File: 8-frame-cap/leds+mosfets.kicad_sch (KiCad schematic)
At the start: 113 parts, among them T1 PHPT610035PKX, T2 PHPT610035PKX, T3 PHPT610035PKX, T4 PHPT610035PKX, T5 PHPT610035PKX, T6 PHPT610035PKX, T7 PHPT610035PKX, U4 SN74AHCT32DBR, U5 SN74AHCT32DBR

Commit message: routed traces, reorganized, renamed
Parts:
- removed D2: 4, LED_SMD:LED_0603_1608Metric, symbol Device:LED
- removed D3, D5, D6: 56, LED_SMD:LED_0603_1608Metric, symbol Device:LED
- removed D4: 5, LED_SMD:LED_0603_1608Metric, symbol Device:LED
- added D10, D28, D52, D58, D64: 23, LED_SMD:LED_0805_2012Metric_Pad1.15x1.40mm_HandSolder, symbol Device:LED
- added D18, D36, D53, D54, D59, D60, D65, D66: 3, LED_SMD:LED_0805_2012Metric_Pad1.15x1.40mm_HandSolder, symbol Device:LED
- added D20, D56, D62: 12, LED_SMD:LED_0805_2012Metric_Pad1.15x1.40mm_HandSolder, symbol Device:LED
- added D43, D55, D61, D67: 1, LED_SMD:LED_0805_2012Metric_Pad1.15x1.40mm_HandSolder, symbol Device:LED
- added D51, D57, D63: 2, LED_SMD:LED_0805_2012Metric_Pad1.15x1.40mm_HandSolder, symbol Device:LED
- added R10, R14, R23, R32, R40, R48, R55, R63, R64, R65, R66, R67, R7, R8, R9: R_Small_US, Resistor_SMD:R_0603_1608Metric_Pad0.98x0.95mm_HandSolder, symbol Device:R_Small_US
- added T8: PHPT610035PKX, GRAD-CAP:PHPT610035PKX_TRANS-2PNP-100V-3A, symbol PHPT610035PKX_TRANS-2PNP-100V-3A:PHPT610035PKX
- added TP1, TP10, TP11, TP12, TP13, TP14, TP15, TP16, TP2, TP3, TP4, TP5, TP6, TP7, TP8, TP9: TestPoint, TestPoint:TestPoint_Loop_D3.80mm_Drill2.5mm, symbol testpoint:TestPoint
- D1, D8: footprint LED_SMD:LED_0603_1608Metric -> LED_SMD:LED_0805_2012Metric_Pad1.15x1.40mm_HandSolder
- D11, D30: value 6 -> 3; footprint LED_SMD:LED_0603_1608Metric -> LED_SMD:LED_0805_2012Metric_Pad1.15x1.40mm_HandSolder
- D12, D23, D24: value 67 -> 3; footprint LED_SMD:LED_0603_1608Metric -> LED_SMD:LED_0805_2012Metric_Pad1.15x1.40mm_HandSolder
- D13: value 56 -> 1; footprint LED_SMD:LED_0603_1608Metric -> LED_SMD:LED_0805_2012Metric_Pad1.15x1.40mm_HandSolder
- D14: value 6 -> 12; footprint LED_SMD:LED_0603_1608Metric -> LED_SMD:LED_0805_2012Metric_Pad1.15x1.40mm_HandSolder
- D15: value 6 -> 2; footprint LED_SMD:LED_0603_1608Metric -> LED_SMD:LED_0805_2012Metric_Pad1.15x1.40mm_HandSolder
- D16: value 1 -> 23; footprint LED_SMD:LED_0603_1608Metric -> LED_SMD:LED_0805_2012Metric_Pad1.15x1.40mm_HandSolder
- D17, D42: value 23 -> 3; footprint LED_SMD:LED_0603_1608Metric -> LED_SMD:LED_0805_2012Metric_Pad1.15x1.40mm_HandSolder
- D19: value 23 -> 1; footprint LED_SMD:LED_0603_1608Metric -> LED_SMD:LED_0805_2012Metric_Pad1.15x1.40mm_HandSolder
- D2: renamed from D10; footprint LED_SMD:LED_0603_1608Metric -> LED_SMD:LED_0805_2012Metric_Pad1.15x1.40mm_HandSolder
- D21: value 67 -> 2; footprint LED_SMD:LED_0603_1608Metric -> LED_SMD:LED_0805_2012Metric_Pad1.15x1.40mm_HandSolder
- D22: value 7 -> 23; footprint LED_SMD:LED_0603_1608Metric -> LED_SMD:LED_0805_2012Metric_Pad1.15x1.40mm_HandSolder
- D25: value 6 -> 1; footprint LED_SMD:LED_0603_1608Metric -> LED_SMD:LED_0805_2012Metric_Pad1.15x1.40mm_HandSolder
- D26: value 32 -> 12; footprint LED_SMD:LED_0603_1608Metric -> LED_SMD:LED_0805_2012Metric_Pad1.15x1.40mm_HandSolder
- D27: value 1 -> 2; footprint LED_SMD:LED_0603_1608Metric -> LED_SMD:LED_0805_2012Metric_Pad1.15x1.40mm_HandSolder
- D29: value 7 -> 3; footprint LED_SMD:LED_0603_1608Metric -> LED_SMD:LED_0805_2012Metric_Pad1.15x1.40mm_HandSolder
- D3: renamed from D20; footprint LED_SMD:LED_0603_1608Metric -> LED_SMD:LED_0805_2012Metric_Pad1.15x1.40mm_HandSolder
- D31: value 7 -> 1; footprint LED_SMD:LED_0603_1608Metric -> LED_SMD:LED_0805_2012Metric_Pad1.15x1.40mm_HandSolder
- D32: value 4 -> 12; footprint LED_SMD:LED_0603_1608Metric -> LED_SMD:LED_0805_2012Metric_Pad1.15x1.40mm_HandSolder
- D33, D45: value 7 -> 2; footprint LED_SMD:LED_0603_1608Metric -> LED_SMD:LED_0805_2012Metric_Pad1.15x1.40mm_HandSolder
- D34: value 3 -> 23; footprint LED_SMD:LED_0603_1608Metric -> LED_SMD:LED_0805_2012Metric_Pad1.15x1.40mm_HandSolder
- D35: value 12 -> 3; footprint LED_SMD:LED_0603_1608Metric -> LED_SMD:LED_0805_2012Metric_Pad1.15x1.40mm_HandSolder
- D37: value 8 -> 1; footprint LED_SMD:LED_0603_1608Metric -> LED_SMD:LED_0805_2012Metric_Pad1.15x1.40mm_HandSolder
- D38: value 67 -> 12; footprint LED_SMD:LED_0603_1608Metric -> LED_SMD:LED_0805_2012Metric_Pad1.15x1.40mm_HandSolder
- D39: value 45 -> 2; footprint LED_SMD:LED_0603_1608Metric -> LED_SMD:LED_0805_2012Metric_Pad1.15x1.40mm_HandSolder
- D4: renamed from D28; footprint LED_SMD:LED_0603_1608Metric -> LED_SMD:LED_0805_2012Metric_Pad1.15x1.40mm_HandSolder
- D40: value 8 -> 23; footprint LED_SMD:LED_0603_1608Metric -> LED_SMD:LED_0805_2012Metric_Pad1.15x1.40mm_HandSolder
- D41: value 8 -> 3; footprint LED_SMD:LED_0603_1608Metric -> LED_SMD:LED_0805_2012Metric_Pad1.15x1.40mm_HandSolder
- D44: value 5 -> 12; footprint LED_SMD:LED_0603_1608Metric -> LED_SMD:LED_0805_2012Metric_Pad1.15x1.40mm_HandSolder
- D46: value 5 -> 23; footprint LED_SMD:LED_0603_1608Metric -> LED_SMD:LED_0805_2012Metric_Pad1.15x1.40mm_HandSolder
- D47: value 5 -> 3; footprint LED_SMD:LED_0603_1608Metric -> LED_SMD:LED_0805_2012Metric_Pad1.15x1.40mm_HandSolder
- D48: value 81 -> 3; footprint LED_SMD:LED_0603_1608Metric -> LED_SMD:LED_0805_2012Metric_Pad1.15x1.40mm_HandSolder
- D49: value 81 -> 1; footprint LED_SMD:LED_0603_1608Metric -> LED_SMD:LED_0805_2012Metric_Pad1.15x1.40mm_HandSolder
- D5: renamed from D36; footprint LED_SMD:LED_0603_1608Metric -> LED_SMD:LED_0805_2012Metric_Pad1.15x1.40mm_HandSolder
- D50: value 81 -> 12; footprint LED_SMD:LED_0603_1608Metric -> LED_SMD:LED_0805_2012Metric_Pad1.15x1.40mm_HandSolder
- D6: renamed from D43; footprint LED_SMD:LED_0603_1608Metric -> LED_SMD:LED_0805_2012Metric_Pad1.15x1.40mm_HandSolder
- D7: value 12 -> 1; footprint LED_SMD:LED_0603_1608Metric -> LED_SMD:LED_0805_2012Metric_Pad1.15x1.40mm_HandSolder
- D9: value 12 -> 2; footprint LED_SMD:LED_0603_1608Metric -> LED_SMD:LED_0805_2012Metric_Pad1.15x1.40mm_HandSolder
- R1: renamed from R14; footprint Resistor_SMD:R_0805_2012Metric_Pad1.20x1.40mm_HandSolder -> Resistor_SMD:R_0603_1608Metric_Pad0.98x0.95mm_HandSolder
- R11, R12, R13: value 10k -> R_Small_US; footprint Capacitor_SMD:C_0805_2012Metric_Pad1.18x1.45mm_HandSolder -> Resistor_SMD:R_0603_1608Metric_Pad0.98x0.95mm_HandSolder
- R15, R16, R17, R18, R19, R20, R21, R22, R24, R25, R26, R27, R28, R29, R30, R31, R33, R34, R35, R36, R37, R38, R39, R41, R42, R43, R44, R45, R46, R47, R49, R50, R51, R52, R53, R54, R56, R57, R58, R59, R60, R61, R62: footprint Resistor_SMD:R_0805_2012Metric_Pad1.20x1.40mm_HandSolder -> Resistor_SMD:R_0603_1608Metric_Pad0.98x0.95mm_HandSolder
- R2: renamed from R23; footprint Resistor_SMD:R_0805_2012Metric_Pad1.20x1.40mm_HandSolder -> Resistor_SMD:R_0603_1608Metric_Pad0.98x0.95mm_HandSolder
- R3: renamed from R32; footprint Resistor_SMD:R_0805_2012Metric_Pad1.20x1.40mm_HandSolder -> Resistor_SMD:R_0603_1608Metric_Pad0.98x0.95mm_HandSolder
- R4: renamed from R40; footprint Resistor_SMD:R_0805_2012Metric_Pad1.20x1.40mm_HandSolder -> Resistor_SMD:R_0603_1608Metric_Pad0.98x0.95mm_HandSolder
- R5: renamed from R48; footprint Resistor_SMD:R_0805_2012Metric_Pad1.20x1.40mm_HandSolder -> Resistor_SMD:R_0603_1608Metric_Pad0.98x0.95mm_HandSolder
- R6: renamed from R55; footprint Resistor_SMD:R_0805_2012Metric_Pad1.20x1.40mm_HandSolder -> Resistor_SMD:R_0603_1608Metric_Pad0.98x0.95mm_HandSolder
- R75: renamed from R8; footprint Capacitor_SMD:C_0805_2012Metric_Pad1.18x1.45mm_HandSolder -> Capacitor_SMD:C_0402_1005Metric_Pad0.74x0.62mm_HandSolder
- R76: renamed from R9; footprint Capacitor_SMD:C_0805_2012Metric_Pad1.18x1.45mm_HandSolder -> Capacitor_SMD:C_0402_1005Metric_Pad0.74x0.62mm_HandSolder
- R77: renamed from R10; footprint Capacitor_SMD:C_0805_2012Metric_Pad1.18x1.45mm_HandSolder -> Capacitor_SMD:C_0402_1005Metric_Pad0.74x0.62mm_HandSolder
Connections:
- net 0: no longer T5.4 (BASE)
- net 1: now also T1.4 (BASE); no longer T2.2 (BASE)
- net 1or2: now also R3.1, R31.1, R41.1, T4.7 (COLLECTOR), T4.8 (COLLECTOR), TP9.1; no longer R2.1, R20.1, R21.1, R22.1, T7.7 (COLLECTOR), T7.8 (COLLECTOR)
- net 2: now also T5.2 (BASE); no longer T1.4 (BASE)
- net 2or3: now also R26.1, R28.1, R42.1, T3.7 (COLLECTOR), T3.8 (COLLECTOR), R23.1, R32.1, TP13.1; no longer R30.1, R31.1, R54.1, T7.5 (COLLECTOR), T7.6 (COLLECTOR)
- net 3: now also T6.2 (BASE); no longer T4.2 (BASE)
- net 4: now also T7.2 (BASE)
- net 5: now also T6.4 (BASE); no longer T3.2 (BASE)
- net 6: now also T7.4 (BASE), U5.9 (3A); no longer T2.4 (BASE)
- net 6or7: now also R13.1, R16.1, R19.1, R44.1, R53.1, R57.1, T4.5 (COLLECTOR), T4.6 (COLLECTOR), R10.1, R63.1, R67.1, R7.1, TP15.1; no longer R25.1, R33.1, R35.2, R36.1, R50.1, T1.7 (COLLECTOR), T1.8 (COLLECTOR)
- net 7: now also U5.10 (3B); no longer T6.2 (BASE)
- net GND: now also D10.1 (K), D18.1 (K), D20.1 (K), D28.1 (K), D36.1 (K), D43.1 (K), D51.1 (K), D52.1 (K), D53.1 (K), D54.1 (K), D55.1 (K), D56.1 (K), D57.1 (K), D58.1 (K), D59.1 (K), D60.1 (K), D61.1 (K), D62.1 (K), D63.1 (K), D64.1 (K), D65.1 (K), D66.1 (K), D67.1 (K); no longer R11.2, R12.2, R13.2
- net f1or2: now also T4.2 (BASE); no longer T7.2 (BASE)
- net f1or8: now also T1.2 (BASE); no longer T6.4 (BASE)
- net f2or3: now also T3.2 (BASE); no longer T7.4 (BASE)
- net f4or5: now also T2.4 (BASE); no longer T4.4 (BASE)
- net f5or6: now also T5.4 (BASE); no longer T5.2 (BASE)
- net f6or7: now also T4.4 (BASE); no longer T1.2 (BASE)
- net frame7: now also TP7.1; no longer R34.1, R41.1, R43.2, R45.1, R57.1, T2.5 (COLLECTOR), T2.6 (COLLECTOR)
- net frame8: now also TP8.1; no longer R49.1, R52.1, R53.1, T6.7 (COLLECTOR), T6.8 (COLLECTOR)
- net at D39.2 (A): now also R39.2; no longer R51.2
- net at R52.2: now also D52.2 (A); no longer D40.2 (A)
- net at R29.2: now also D29.2 (A); no longer D16.2 (A)
- net at R27.2: now also D27.2 (A); no longer D14.2 (A)
- net at R57.2: now also D57.2 (A); no longer D45.2 (A)
- net at R20.2: now also D20.2 (A); no longer D7.2 (A)
- net at D32.2 (A): now also R32.2; no longer R44.2
- net at D38.2 (A): now also R38.2; no longer R50.2
- net f7or8: now reaches T3.4 (BASE)
- net f7or8: now also U5.8 (3Y)
- net at D13.2 (A): now also R13.2; no longer R26.1
- net at R53.2: now also D53.2 (A); no longer D41.2 (A)
- net at D24.2 (A): now also R24.2; no longer R36.2
- net at R15.2: now also D15.2 (A)
- net at D48.2 (A): now also R48.2; no longer R60.2
- net at R42.2: now also D42.2 (A); no longer D30.2 (A)
- net at R62.2: now also D62.2 (A); no longer D50.2 (A)
- net at R25.2: now also D25.2 (A); no longer D12.2 (A)
- net at R28.2: now also D28.2 (A); no longer D15.2 (A)
- net at R54.2: now also D54.2 (A); no longer D42.2 (A)
- net at D17.2 (A): now also R17.2; no longer R30.2
- net at D8.2 (A): now also R8.2; no longer R21.2
- net at D21.2 (A): now also R21.2; no longer R33.2
- net at R41.2: now also D41.2 (A); no longer D29.2 (A)
- net at R49.2: now also D49.2 (A); no longer D37.2 (A)
- net at D33.2 (A): now also R33.2; no longer R45.2
- net at R56.2: now also D56.2 (A); no longer D44.2 (A)
- net at R59.2: now also D59.2 (A); no longer D47.2 (A)
- net at D34.2 (A): now also R34.2; no longer R46.2
- net at D11.2 (A): now also R11.2; no longer R24.2
- net at D22.2 (A): now also R22.2; no longer R34.2
- net at D35.2 (A): now also R35.2; no longer R47.2
- net at R19.2: now also D19.2 (A)
- net at D23.2 (A): now also R23.2; no longer R35.1
- net at D9.2 (A): now also R9.2; no longer R22.2
- net at R37.2: now also D37.2 (A); no longer D25.2 (A)
- net at R18.2: now also D18.2 (A)
- net 6c: now reaches R17.1
- net 6c: now also R1.1, R11.1, R20.1, R24.1, R45.1, T3.5 (COLLECTOR), T3.6 (COLLECTOR), R14.1, R8.1, TP12.1
- net at R61.2: now also D61.2 (A); no longer D49.2 (A)
- net at R31.2: now also D31.2 (A); no longer D19.2 (A)
- net 3c: now reaches R43.1
- net 3c: now also R27.1, R29.1, R33.1, R39.1, R5.1, T2.7 (COLLECTOR), T2.8 (COLLECTOR), TP10.1; no longer D31.2 (A)
- net at D46.2 (A): now also R46.2; no longer R58.1
- net at D26.2 (A): now also R26.2; no longer R38.2
- net at R16.2: now also D16.2 (A)
- removed net 4or5: R51.1, T4.5 (COLLECTOR), T4.6 (COLLECTOR)
- removed net 5or6: R16.1, R18.1, R19.1, R26.2, T5.7 (COLLECTOR), T5.8 (COLLECTOR)
- removed net 8or1: R60.1, R61.1, R62.1, T6.5 (COLLECTOR), T6.6 (COLLECTOR)
- removed net frame1: R1.1, R29.1, R39.1, T5.5 (COLLECTOR), T5.6 (COLLECTOR)
- removed net frame2: R3.1, T2.7 (COLLECTOR), T2.8 (COLLECTOR)
- removed net frame3: R46.1, R5.1, R6.1, T1.5 (COLLECTOR), T1.6 (COLLECTOR)
- removed net frame4: R15.1, R44.1, T4.7 (COLLECTOR), T4.8 (COLLECTOR)
- removed net frame5: R17.2, R56.1, R58.2, R59.1, T3.5 (COLLECTOR), T3.6 (COLLECTOR)
- removed net frame6: R24.1, R27.1, R28.1, R37.1, R42.1, T3.7 (COLLECTOR), T3.8 (COLLECTOR)
- removed net u8-pd2a: R13.1, U5.10 (3B)
- net u8-pd2b renamed 1c
- net 1c: now also R15.1, R18.1, R2.1, R46.1, T1.7 (COLLECTOR), T1.8 (COLLECTOR), R9.1, TP16.1; no longer U5.9 (3A)
- removed net u8-pd2y: R11.1, U5.8 (3Y)
- new net: D63.2 (A), R63.2
- new net: D66.2 (A), R66.2
- new net: D43.2 (A), R43.2
- new net: D44.2 (A), R44.2
- new net: D64.2 (A), R64.2
- new net: D10.2 (A), R10.2
- new net: D36.2 (A), R36.2
- new net: D47.2 (A), R47.2
- new net: D55.2 (A), R55.2
- new net: D67.2 (A), R67.2
- new net: D60.2 (A), R60.2
- new net: D7.2 (A), R7.2
- new net: D58.2 (A), R58.2
- new net: D50.2 (A), R50.2
- new net: D65.2 (A), R65.2
- new net: D45.2 (A), R45.2
- new net: D30.2 (A), R30.2
- new net: D40.2 (A), R40.2
- new net: D14.2 (A), R14.2
- new net: D51.2 (A), R51.2
- new net: D12.2 (A), R12.2
- new net 10c: R22.1, R52.1, R56.1, R59.1, R62.1, R66.1, T5.5 (COLLECTOR), T5.6 (COLLECTOR), TP11.1
- new net 11c: R34.1, R35.1, R49.1, T6.7 (COLLECTOR), T6.8 (COLLECTOR), TP3.1
- new net 12c: R58.1, T6.5 (COLLECTOR), T6.6 (COLLECTOR), TP5.1
- new net 13c: R36.1, R50.1, R54.1, R64.1, T7.7 (COLLECTOR), T7.8 (COLLECTOR), TP4.1
- new net 14c: R60.1, T7.5 (COLLECTOR), T7.6 (COLLECTOR), TP6.1
- new net 15b: T8.2 (BASE)
- new net 15c: T8.7 (COLLECTOR), T8.8 (COLLECTOR)
- new net 16b: T8.4 (BASE)
- new net 16c: T8.5 (COLLECTOR), T8.6 (COLLECTOR)
- new net 2c: R25.1, R37.1, T1.5 (COLLECTOR), T1.6 (COLLECTOR), TP1.1
- new net 4c: R21.1, R30.1, R40.1, R51.1, R55.1, R6.1, R61.1, R65.1, T2.5 (COLLECTOR), T2.6 (COLLECTOR), TP14.1
- new net 9c: R48.1, T5.7 (COLLECTOR), T5.8 (COLLECTOR), TP2.1
- new net f3or4: T2.2 (BASE)
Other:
- note added: "base"
- note added: "collector"
- moved on the sheet: D1, D2, D3, D4, D5, D6, R1, R2, R3, R4, R5, R6

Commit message: updated pcb
error checking
90* angles removal
schematic relinking
reorganizing schematic
fixed footprints for PHPT6 (mosfets, they didnt like the pads and the body being "different" pours or something)
silkscreen reorg
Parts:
- removed R75, R76, R77: 10k, Capacitor_SMD:C_0402_1005Metric_Pad0.74x0.62mm_HandSolder, symbol Device:R_Small_US
- removed T1, T2, T3, T4, T5, T6, T7, T8: PHPT610035PKX, GRAD-CAP:PHPT610035PKX_TRANS-2PNP-100V-3A, symbol PHPT610035PKX_TRANS-2PNP-100V-3A:PHPT610035PKX
- removed TP1, TP10, TP11, TP12, TP13, TP14, TP15, TP16, TP2, TP3, TP4, TP5, TP6, TP7, TP8, TP9: TestPoint, TestPoint:TestPoint_Loop_D3.80mm_Drill2.5mm, symbol testpoint:TestPoint
- removed U4, U5: SN74AHCT32DBR, GRAD-CAP:SN74AHCT32DBR_2-INPUT-QUAD-OR, symbol SN74AHCT32DBR_2-INPUT-QUAD-OR:SN74AHCT32DBR
- D1, D13, D19, D25, D31, D37, D43, D49, D55, D61, D67, D7: value 1 -> ~
- D10, D16, D22, D28, D34, D4, D40, D46, D52, D58, D64: value 23 -> ~
- D11, D12, D17, D18, D23, D24, D29, D30, D35, D36, D41, D42, D47, D48, D5, D53, D54, D59, D6, D60, D65, D66: value 3 -> ~
- D14, D2, D20, D26, D32, D38, D44, D50, D56, D62, D8: value 12 -> ~
- D15, D21, D27, D3, D33, D39, D45, D51, D57, D63, D9: value 2 -> ~
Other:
- note removed: "2-INPUT-QUAD-OR"
- note removed: "MOSFETS"
- note removed: "OR GATES"
- moved on the sheet: D1, D10, D11, D12, D13, D14, D15, D16, D17, D18, D19, D2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

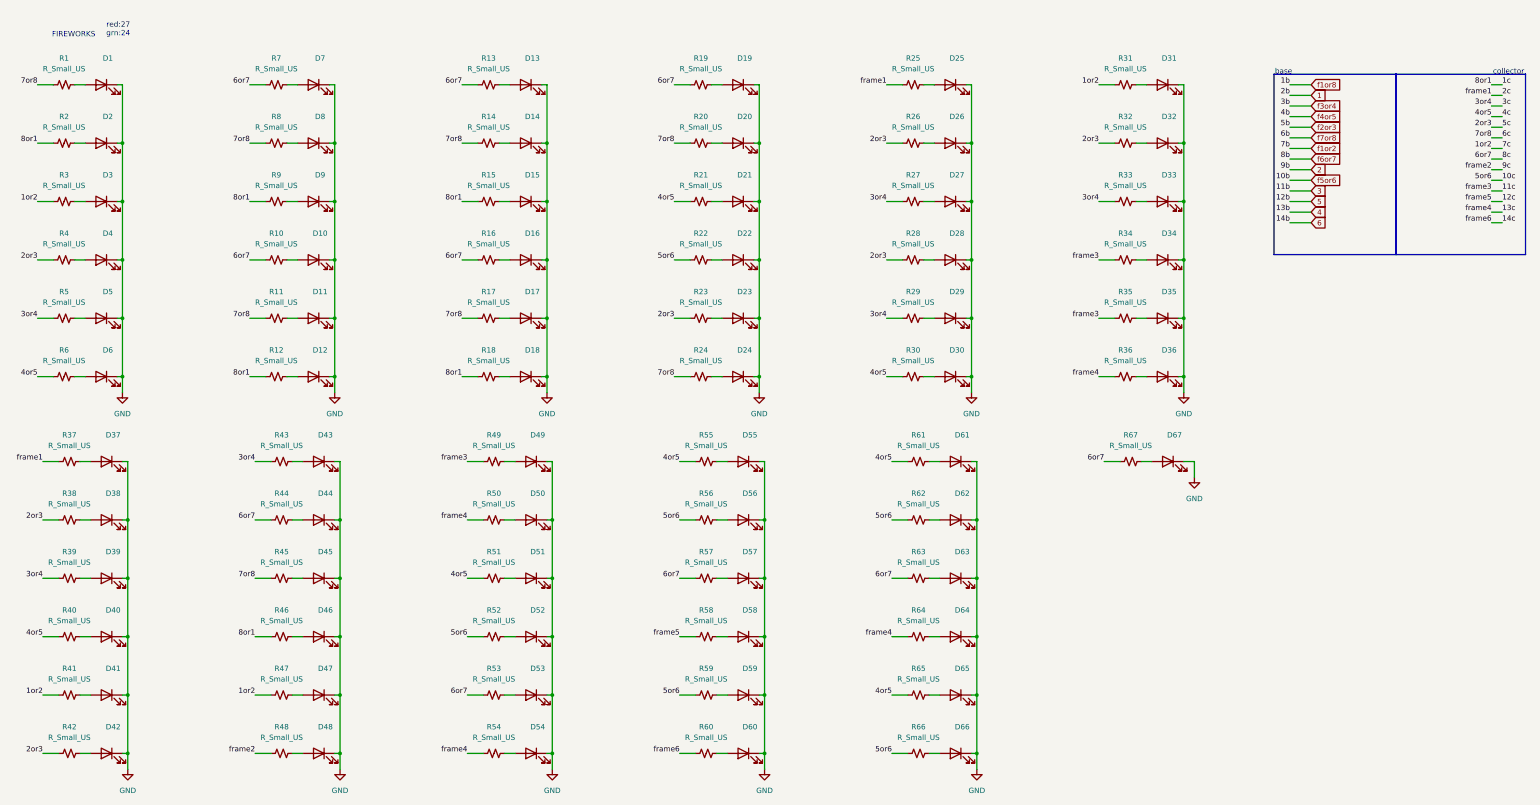
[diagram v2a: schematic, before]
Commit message: updated pcb
shrunk edge cuts
moved led matrix header (again)
added 3d file links
added mounting holes
added 3 on board buttons
fixed unused pin header connections
discovered polygon filled area default chamfer (i will be using this always now)
updated bom with new caps
added status LED for usbc power in
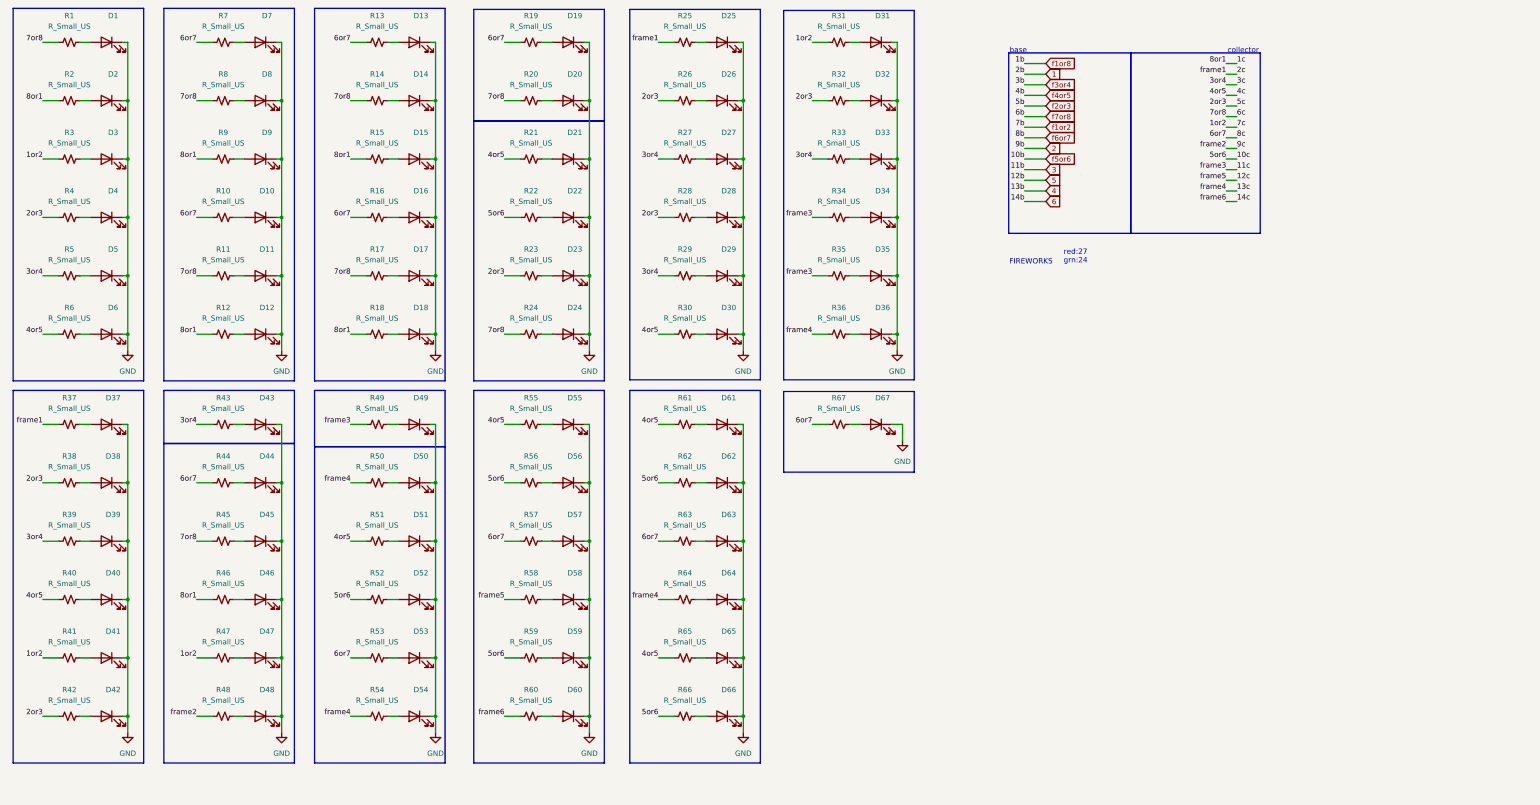
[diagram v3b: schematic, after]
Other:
- moved on the sheet: D1, D10, D11, D12, D13, D14, D15, D16, D17, D18, D19, D2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

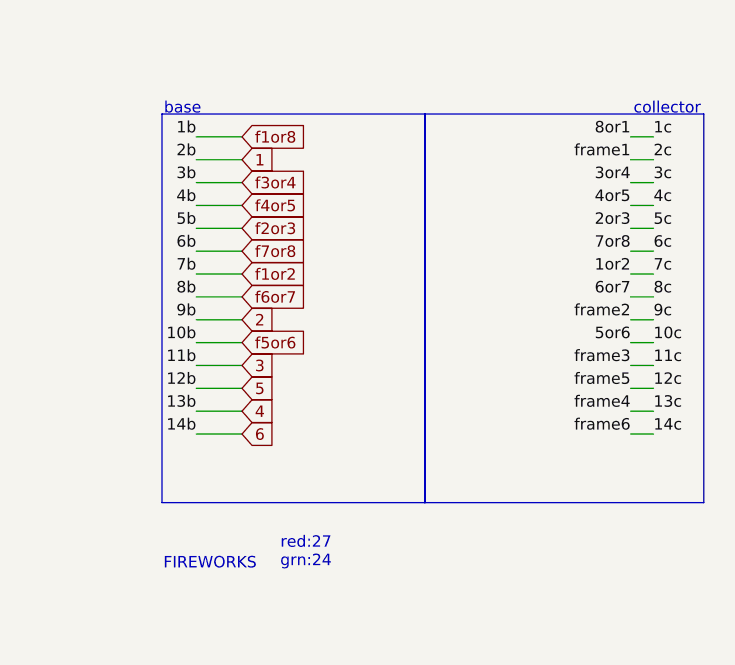
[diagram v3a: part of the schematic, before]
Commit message: updated from prototyping
- jk ff -> incrementer
- shrink to be cap size
- rename labels to match layout
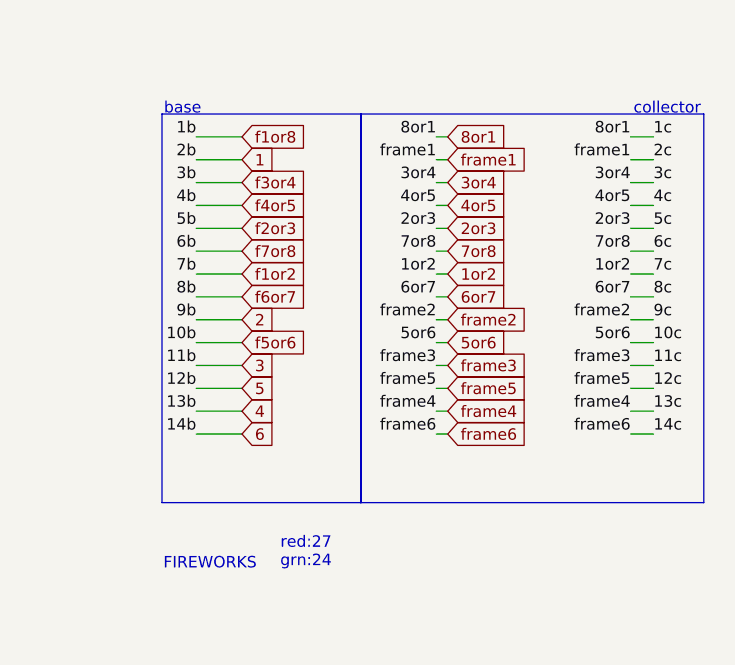
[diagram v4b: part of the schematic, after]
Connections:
- net 10c renamed 5or6
- net 11c renamed frame3
- net 12c renamed frame5
- net 13c renamed frame4
- net 14c renamed frame6
- net 1c renamed 8or1
- net 2c renamed frame1
- net 3c renamed 3or4
- net 4c renamed 4or5
- net 6c renamed 7or8
- net 9c renamed frame2

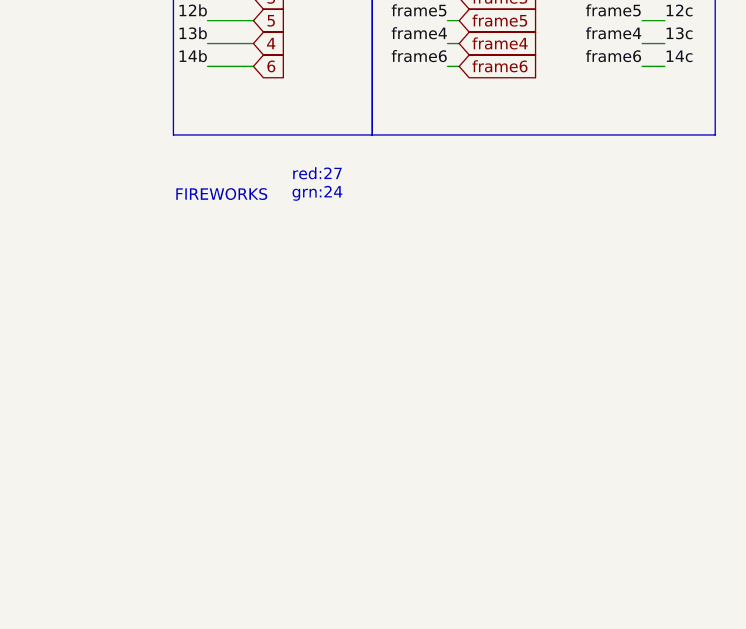
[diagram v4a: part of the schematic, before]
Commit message: updated pcb
added labels for each diode
changed silkscreen to be handwriting
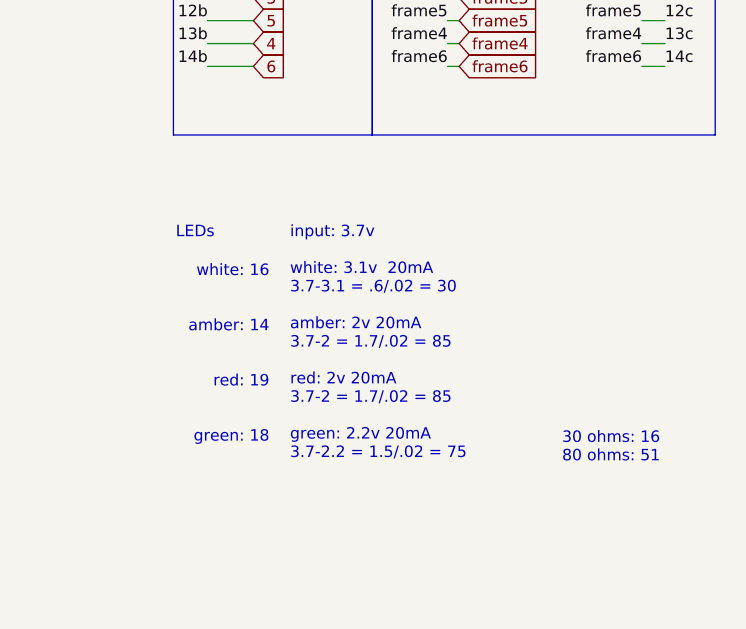
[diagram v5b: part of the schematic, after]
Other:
- note added: "30 ohms: 16 80 ohms: 51"
- note added: "LEDs"
- note added: "input: 3.7v white: 3.1v 20mA 3.7-3.1 = .6/.02 = 30 amber: 2v 20mA 3.7-2 = 1.7/.02 = 85 red: 2v 20mA 3.7-2 = 1.7/.02 = 85 green: 2.2v 20mA 3.7-2.2 = 1.5/.02 = 75"
- note added: "white: 16 amber: 14 red: 19 green: 18"
- note removed: "FIREWORKS"
- note removed: "red:27 grn:24"
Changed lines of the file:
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@@
 		(fill
 			(type color)
-			(color 65 152 255 0.17)
+			(color 255 0 1 0.168627451)
 		)
 	)
@@
 		(fill
 			(type color)
-			(color 65 152 255 0.17)
+			(color 255 0 1 0.17)
 		)
 	)
@@
 		(fill
 			(type color)
-			(color 65 152 255 0.17)
+			(color 255 0 1 0.168627451)
 		)
 	)
@@
 		(fill
 			(type color)
-			(color 65 152 255 0.17)
+			(color 255 0 1 0.168627451)
 		)
 	)
@@
 		)
 	)
-	(text "red:27\ngrn:24"
-		(exclude_from_sim no)
-		(at 270.002 74.168 0)
-		(effects
-			(font
-				(size 1.27 1.27)
-			)
+	(text "white: 16\n\n\namber: 14\n\n\nred: 19\n\n\ngreen: 18"
+		(exclude_from_sim no)
+		(at 264.668 83.058 0)
+		(effects
+			(font
+				(size 1.27 1.27)
+			)
+			(justify right top)
 		)
 	)
@@
 		)
 	)
+	(text "input: 3.7v  \n\nwhite: 3.1v  20mA\n3.7-3.1 = .6/.02 = 30\n\namber: 2v 20mA\n3.7-2 = 1.7/.02 = 85\n\nred: 2v 20mA\n3.7-2 = 1.7/.02 = 85\n\ngreen: 2.2v 20mA\n3.7-2.2 = 1.5/.02 = 75\n"
+		(exclude_from_sim no)
+		(at 266.954 78.74 0)
+		(effects
+			(font
+				(size 1.27 1.27)
+			)
+			(justify left top)
+		)
+	)
 	(text "collector"
 		(exclude_from_sim no)
@@
 		)
 	)
-	(text "FIREWORKS"
-		(exclude_from_sim no)
-		(at 259.334 75.438 0)
-		(effects
-			(font
-				(size 1.27 1.27)
-			)
-		)
-	)
+	(text "LEDs\n"
+		(exclude_from_sim no)
+		(at 254.254 78.74 0)
+		(effects
+			(font
+				(size 1.27 1.27)
+			)
+			(justify left top)
+		)
+	)
+	(text "30 ohms: 16\n80 ohms: 51\n\n"
+		(exclude_from_sim no)
+		(at 297.18 101.6 0)
+		(effects
+			(font
+				(size 1.27 1.27)
+			)
+			(justify left top)
+		)
+	)

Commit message: final push
inverters for pmos
resistors for mux
silkscreen looking fire as hell honestly
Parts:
- renumbered D36 to D1, D24 to D10, D38 to D11, D37 to D12, D39 to D13, D57 to D14, D40 to D15, D15 to D16, D18 to D17, D23 to D18, D25 to D19, D33 to D2, D26 to D20, D41 to D21, D42 to D22, D56 to D23, D55 to D24, D60 to D25, D59 to D26, D13 to D27, D14 to D28, D27 to D29, D32 to D3, D16 to D30, D17 to D31, D22 to D32, D52 to D33, D43 to D34, D51 to D35, D58 to D36, D50 to D37, D49 to D38, D54 to D39, D34 to D4, D61 to D40, D62 to D41, D12 to D42, D11 to D43, D10 to D44, D19 to D45, D5 to D46, D6 to D47, D20 to D48, D53 to D49, D35 to D5, D47 to D50, D64 to D51, D48 to D52, D65 to D53, D63 to D54, D8 to D55, D7 to D56, D4 to D57, D21 to D58, D46 to D59, D30 to D6, D67 to D60, D66 to D61, D9 to D62, D3 to D63, D2 to D64, D45 to D65, D1 to D66, D44 to D67, D29 to D7, D28 to D8, D31 to D9, R36 to R1, R31 to R10, R57 to R11, R38 to R12, R39 to R13, R40 to R14, R26 to R15, R23 to R16, R18 to R17, R25 to R18, R24 to R19, R32 to R2, R41 to R20, R42 to R21, R43 to R22, R56 to R23, R55 to R24, R59 to R25, R60 to R26, R13 to R27, R15 to R28, R14 to R29, R33 to R3, R16 to R30, R17 to R31, R27 to R32, R22 to R33, R52 to R34, R51 to R35, R50 to R36, R58 to R37, R49 to R38, R54 to R39, R34 to R4, R61 to R40, R62 to R41, R12 to R42, R11 to R43, R10 to R44, R6 to R45, R19 to R46, R20 to R47, R53 to R48, R48 to R49, R35 to R5, R64 to R50, R63 to R51, R8 to R52, R7 to R53, R21 to R54, R4 to R55, R5 to R56, R47 to R57, R66 to R58, R65 to R59, R30 to R6, R9 to R60, R3 to R61, R46 to R62, R67 to R63, R2 to R64, R1 to R65, R45 to R66, R44 to R67, R29 to R7, R28 to R8, R37 to R9

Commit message: final push
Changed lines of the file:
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@@
-	)
-	(rectangle
-		(start 16.764 56.388)
-		(end 46.228 70.358)
-		(stroke
-			(width -0.0001)
-			(type solid)
-		)
-		(fill
-			(type color)
-			(color 255 41 77 0.44)
-		)
 	)
 	(rectangle
